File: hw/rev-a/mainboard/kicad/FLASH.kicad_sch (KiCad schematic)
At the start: 5 parts, among them SW6 BOOTSEL, U22 W25Q128JVS

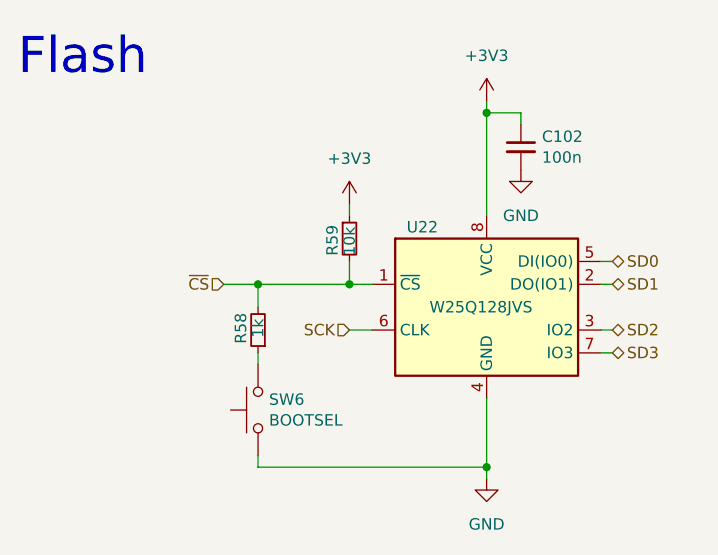
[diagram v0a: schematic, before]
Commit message: hw: ren rev-c -> rev-a
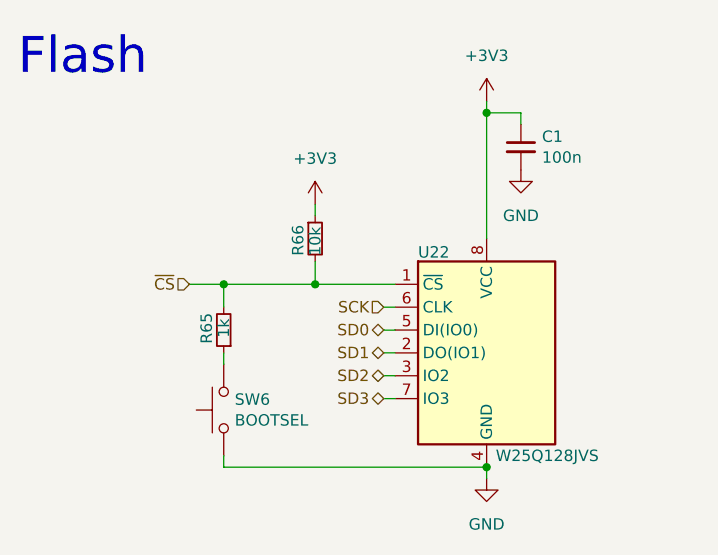
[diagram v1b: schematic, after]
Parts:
- SW6: footprint JLCPCB:SW-TH_L6.0-W3.5-P6.50 -> EconoPET:SW_PUSH_1P1T_6x3.5mm_H4.3_APEM_MJTP1243
- U22: footprint Package_SO:SOIC-8_5.23x5.23mm_P1.27mm -> EconoPET:SOIC-8_5.23x5.23mm_P1.27mm
- renumbered C102 to C1, R58 to R65, R59 to R66
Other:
- moved on the sheet: R65, R66, SW6, U22

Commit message: hw: tidy rev. a schematics
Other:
- note removed: "Flash"
- moved on the sheet: C1, R65, R66, SW6, U22
